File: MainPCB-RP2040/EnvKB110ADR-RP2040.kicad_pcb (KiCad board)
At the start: 2 copper layers, 429.5 x 125 mm, 264 parts, among them J2 EVQPU, J5 Conn_01x03_Male, U1 TLV75533PDBVR, U3 RP2040, Y1 3225_4P

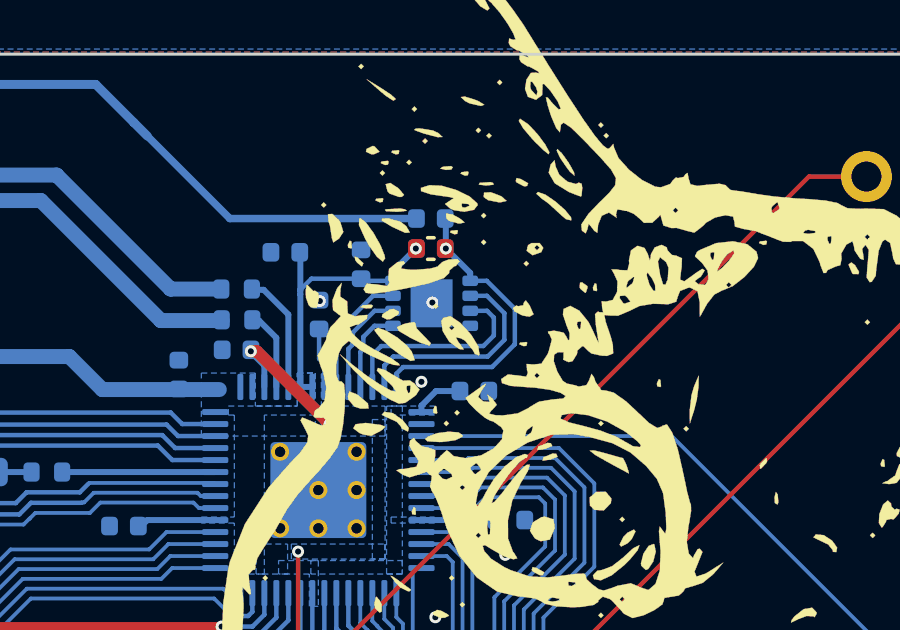
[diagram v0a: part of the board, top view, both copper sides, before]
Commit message: corrections to design, via in pad and such
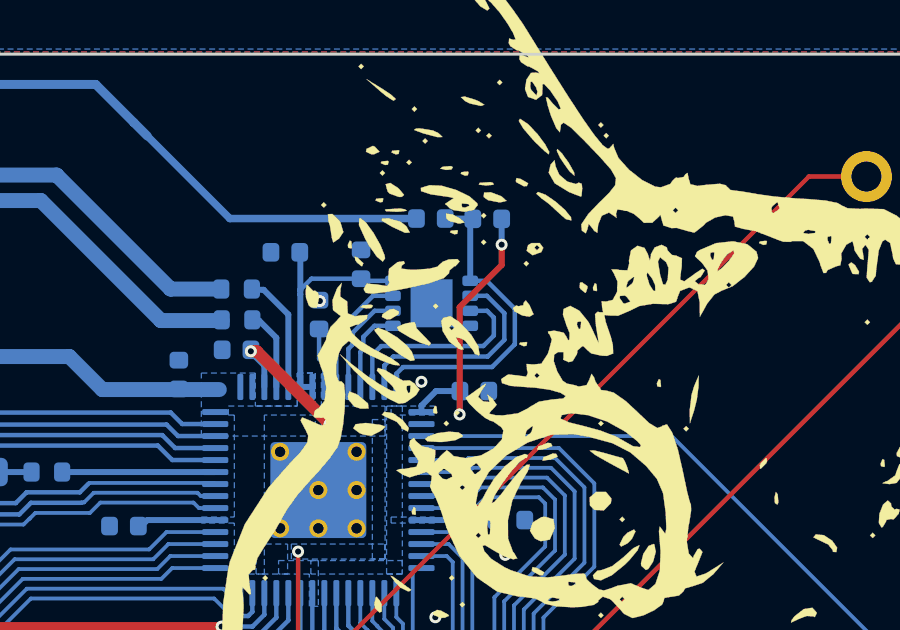
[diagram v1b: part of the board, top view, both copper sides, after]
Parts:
- R2: value DNF -> 10K 0402; moved to B.Cu
- moved R2 2.12 mm to (432.4, 57.0), turned to 180 degrees
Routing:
- net +3V3: track 38.6 -> 45.1 mm, vias 2 -> 3
- net GND: track 15.5 -> 17.1 mm, vias 39 -> 38
- net /QSPI_SS: track 10.3 -> 10.9 mm, vias 1 -> 0

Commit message: added logo for black cat plastic works, couple urls and some fixes to design
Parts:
- added G***: LOGO, logo:adamk, F.Cu at (445.6, 67.8)
- added H11: MountingHole, MountingHole:MountingHole_2.2mm_M2_Pad, F.Cu at (60.1, 54.7)
- added H18: MountingHole, MountingHole:MountingHole_2.2mm_M2_Pad, F.Cu at (387.0, 153.2)
- G***: footprint logo:logo -> logo:lyra
- PWRLED1, R12: moved to F.Cu
- moved G*** 39.1 mm to (406.4, 66.2)
- moved H13 28.4 mm to (387.5, 99.1)
- moved PWRLED1 11.0 mm to (387.1, 54.2), turned to 270 degrees
- moved R12 6.04 mm to (387.1, 57.2), turned to 270 degrees
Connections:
- U3 pad 2: (no net) -> /GPIO0
- USB1 pad 3: (no net) -> Net-(USB1-Pad3)
- USB1 pad 9: (no net) -> Net-(USB1-Pad9)
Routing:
- net VBUS: track 11.1 -> 18.2 mm
- net GND: track 17.1 -> 18.3 mm
- net /RUN: track 36.3 -> 37.0 mm
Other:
- board text added: "BlackCatPlasticWorks.com"
